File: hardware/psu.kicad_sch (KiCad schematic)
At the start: 57 parts, among them J6 Barrel_Jack_Switch, Q3 CSD87503Q3E, Q4 CSD87503Q3E, U10 TLV62569ADRL, U4 TPS61022, U5 BQ25798RQMR

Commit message: Debugging LED added
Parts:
- R10, R11, R34, R35, R37, R38, R39, R40, R41, R42, R_INT1, R_QON1, R_SCL1, R_SDA1, R_TS1, R_TS3: footprint Resistor_SMD:R_0603_1608Metric -> Resistor_SMD:R_0805_2012Metric
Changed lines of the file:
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@@
 			)
 		)
-		(property "Footprint" "Resistor_SMD:R_0603_1608Metric"
+		(property "Footprint" "Resistor_SMD:R_0805_2012Metric"
 			(at 196.088 64.77 90)
 			(effects
@@
 			)
 		)
-		(property "Footprint" "Resistor_SMD:R_0603_1608Metric"
+		(property "Footprint" "Resistor_SMD:R_0805_2012Metric"
 			(at 199.898 36.83 90)
 			(effects
@@
 			)
 		)
-		(property "Footprint" "Resistor_SMD:R_0603_1608Metric"
+		(property "Footprint" "Resistor_SMD:R_0805_2012Metric"
 			(at 76.2 68.072 90)
 			(effects
@@
 			)
 		)
-		(property "Footprint" "Resistor_SMD:R_0603_1608Metric"
+		(property "Footprint" "Resistor_SMD:R_0805_2012Metric"
 			(at 82.042 173.99 90)
 			(effects
@@
 			)
 		)
-		(property "Footprint" "Resistor_SMD:R_0603_1608Metric"
+		(property "Footprint" "Resistor_SMD:R_0805_2012Metric"
 			(at 31.242 55.88 90)
 			(effects
@@
 			)
 		)
-		(property "Footprint" "Resistor_SMD:R_0603_1608Metric"
+		(property "Footprint" "Resistor_SMD:R_0805_2012Metric"
 			(at 179.832 148.59 90)
 			(effects
@@
 			)
 		)
-		(property "Footprint" "Resistor_SMD:R_0603_1608Metric"
+		(property "Footprint" "Resistor_SMD:R_0805_2012Metric"
 			(at 82.042 185.42 90)
 			(effects
@@
 			)
 		)
-		(property "Footprint" "Resistor_SMD:R_0603_1608Metric"
+		(property "Footprint" "Resistor_SMD:R_0805_2012Metric"
 			(at 98.552 101.6 90)
 			(effects
@@
 			)
 		)
-		(property "Footprint" "Resistor_SMD:R_0603_1608Metric"
+		(property "Footprint" "Resistor_SMD:R_0805_2012Metric"
 			(at 256.032 29.21 90)
 			(effects
@@
 			)
 		)
-		(property "Footprint" "Resistor_SMD:R_0603_1608Metric"
+		(property "Footprint" "Resistor_SMD:R_0805_2012Metric"
 			(at 120.142 101.6 90)
 			(effects
@@
 			)
 		)
-		(property "Footprint" "Resistor_SMD:R_0603_1608Metric"
+		(property "Footprint" "Resistor_SMD:R_0805_2012Metric"
 			(at 179.832 137.16 90)
 			(effects
@@
 			)
 		)
-		(property "Footprint" "Resistor_SMD:R_0603_1608Metric"
+		(property "Footprint" "Resistor_SMD:R_0805_2012Metric"
 			(at 187.96 46.482 90)
 			(effects
@@
 			)
 		)
-		(property "Footprint" "Resistor_SMD:R_0603_1608Metric"
+		(property "Footprint" "Resistor_SMD:R_0805_2012Metric"
 			(at 265.43 23.622 90)
 			(effects
@@
 			)
 		)
-		(property "Footprint" "Resistor_SMD:R_0603_1608Metric"
+		(property "Footprint" "Resistor_SMD:R_0805_2012Metric"
 			(at 131.572 101.6 90)
 			(effects
@@
 			)
 		)
-		(property "Footprint" "Resistor_SMD:R_0603_1608Metric"
+		(property "Footprint" "Resistor_SMD:R_0805_2012Metric"
 			(at 108.712 101.6 90)
 			(effects
@@
 			)
 		)
-		(property "Footprint" "Resistor_SMD:R_0603_1608Metric"
+		(property "Footprint" "Resistor_SMD:R_0805_2012Metric"
 			(at 76.2 20.828 90)
 			(effects

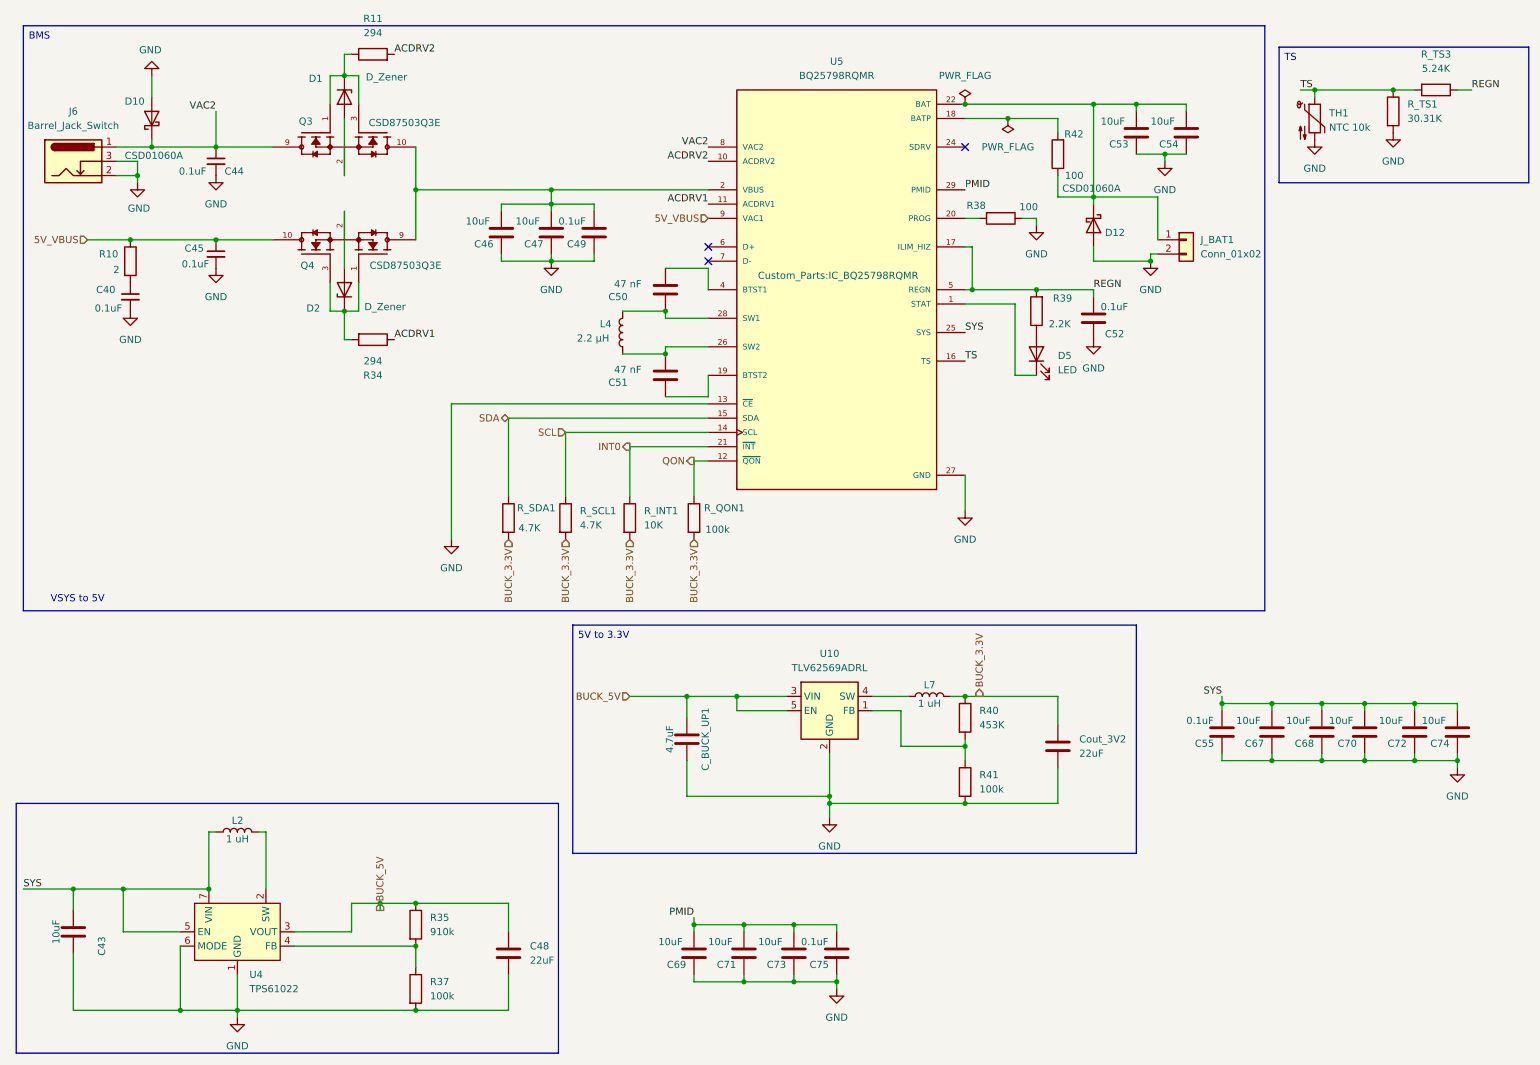
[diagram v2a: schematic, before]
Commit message: Added thermistor connection
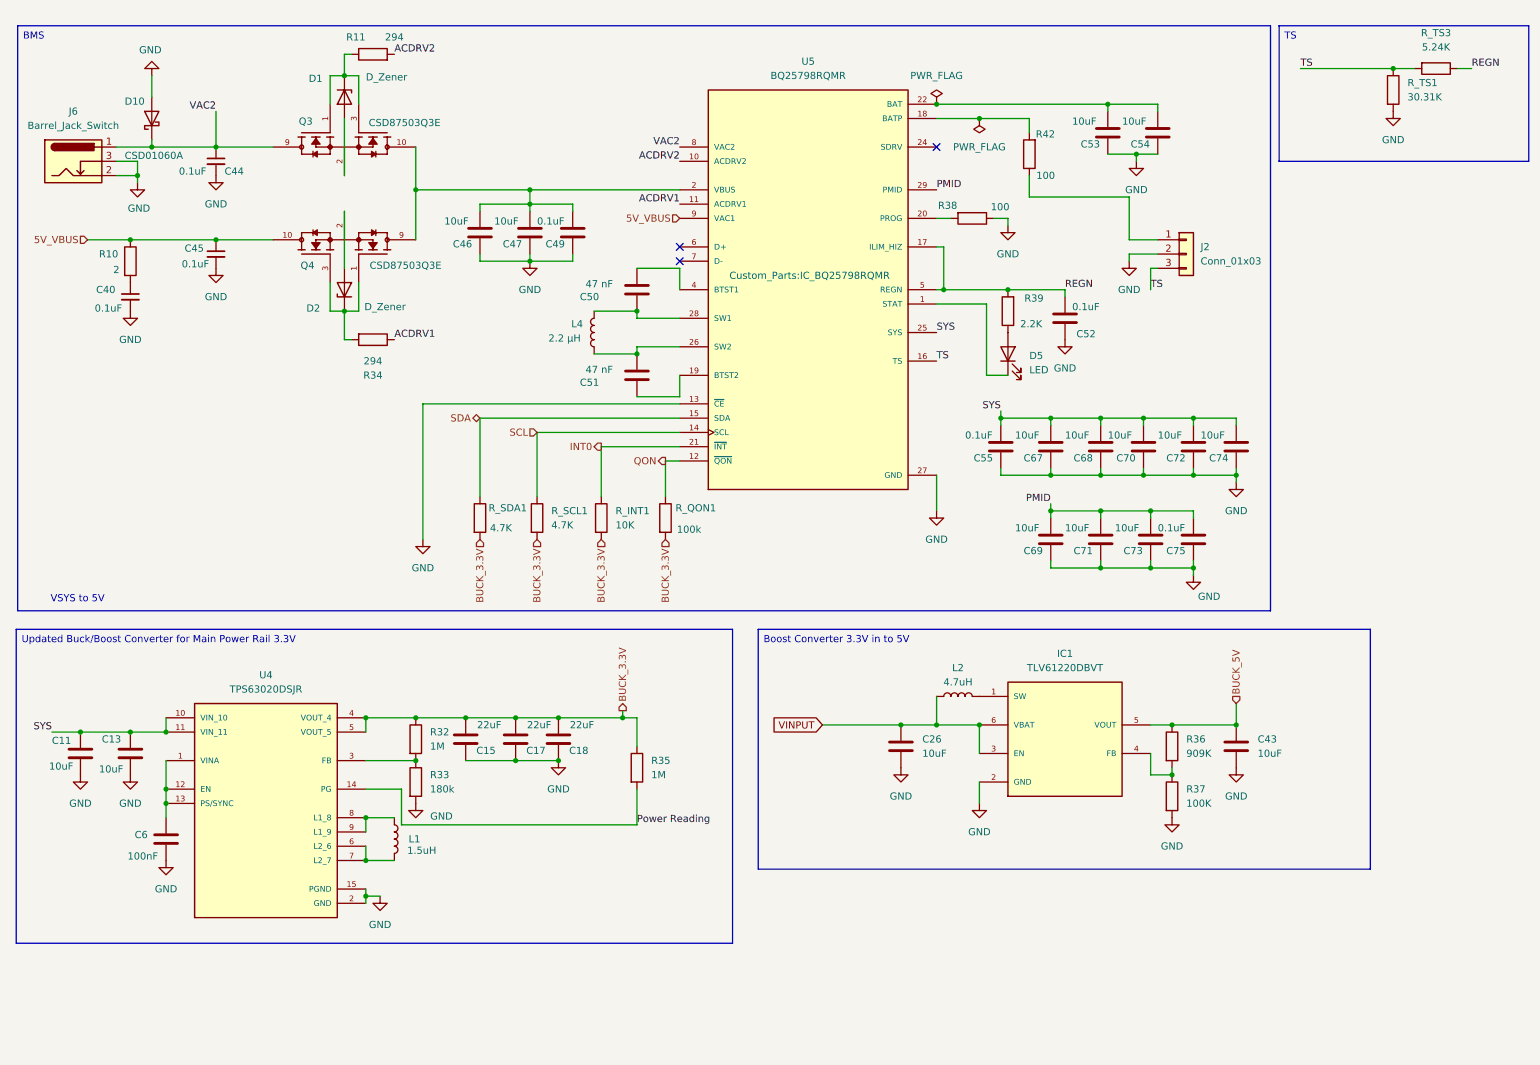
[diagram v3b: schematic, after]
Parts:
- removed C48, Cout_3V2: 22uF, Capacitor_SMD:C_0603_1608Metric, symbol Device:C
- removed C_BUCK_UP1: 4.7uF, Capacitor_SMD:C_0603_1608Metric, symbol Device:C
- removed D12: CSD01060A, Package_TO_SOT_THT:TO-220-2_Vertical, symbol Diode:CSD01060A
- removed J_BAT1: Conn_01x02, Connector_PinHeader_1.27mm:PinHeader_1x02_P1.27mm_Vertical, symbol Connector_Generic:Conn_01x02
- removed L7: 1 uH, Inductor_SMD:L_7.3x7.3_H3.5, symbol Device:L
- removed R40: 453K, Resistor_SMD:R_0805_2012Metric, symbol Device:R
- removed R41: 100k, Resistor_SMD:R_0805_2012Metric, symbol Device:R
- removed TH1: NTC 10k, Resistor_SMD:R_0603_1608Metric, symbol Device:Thermistor_NTC
- removed U10: TLV62569ADRL, Package_TO_SOT_SMD:SOT-563, symbol Regulator_Switching:TLV62569ADRL
- removed U4: TPS61022, Package_DFN_QFN:Texas_RWU0007A_VQFN-7_2x2mm_P0.5mm, symbol Converter_DCDC:TPS61022
- added C11, C13, C26: 10uF, symbol Device:C
- added C15, C17, C18: 22uF, symbol Device:C
- added C6: 100nF, symbol Device:C
- added IC1: TLV61220DBVT, symbol TLV61220DBVT:TLV61220DBVT
- added J2: Conn_01x03, Connector_JST:JST_PH_S3B-PH-K_1x03_P2.00mm_Horizontal, symbol Connector_Generic:Conn_01x03
- added L1: 1.5uH, symbol Device:L
- added R32: 1M, symbol Device:R
- added R33: 180k, symbol Device:R
- added R36: 909K, symbol Device:R
- added U4: TPS63020DSJR, TPS63020DSJR:IC_TPS63020DSJR, symbol TPS63020DSJR:TPS63020DSJR
- C43: footprint Capacitor_SMD:C_0603_1608Metric -> (none)
- L2: value 1 uH -> 4.7uH; footprint Inductor_SMD:L_7.3x7.3_H3.5 -> (none)
- R35: value 910k -> 1M; footprint Resistor_SMD:R_0805_2012Metric -> (none)
- R37: value 100k -> 100K; footprint Resistor_SMD:R_0805_2012Metric -> (none)
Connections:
- net BAT: no longer R42.1
- net BUCK_3.3V: now also R35.1, C15.2, C17.2, C18.2, R32.1, U4.4 (VOUT_4), U4.5 (VOUT_5)
- net BUCK_5V: now also C43.1, IC1.5 (VOUT), R36.1; no longer R35.1
- net GND: now also C11.2, C13.2, C15.1, C17.1, C18.1, C26.2, C6.2, IC1.2 (GND), J2.2 (Pin_2), R33.2, U4.15 (PGND), U4.2 (GND)
- net SYS: now also C11.1, C13.1, U4.10 (VIN_10), U4.11 (VIN_11); no longer C43.1, L2.1
- net TS: now also J2.3 (Pin_3)
- net at L2.2: now also IC1.1 (SW)
- net at R37.1: now also IC1.4 (FB), R36.2; no longer R35.2
- new net: J2.1 (Pin_1), R42.1
- new net: R32.2, R33.1, U4.3 (FB)
- new net: C6.1, U4.1 (VINA), U4.12 (EN), U4.13 (PS/SYNC)
- new net: L1.1, U4.8 (L1_8), U4.9 (L1_9)
- new net: L1.2, U4.6 (L2_6), U4.7 (L2_7)
- new net Power Reading: R35.2, U4.14 (PG)
- new net VINPUT: C26.1, IC1.3 (EN), IC1.6 (VBAT), L2.1
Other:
- moved on the sheet: C46, C47, C49, C50, C51, C52, C53, C54, C55, C67, C68, C69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

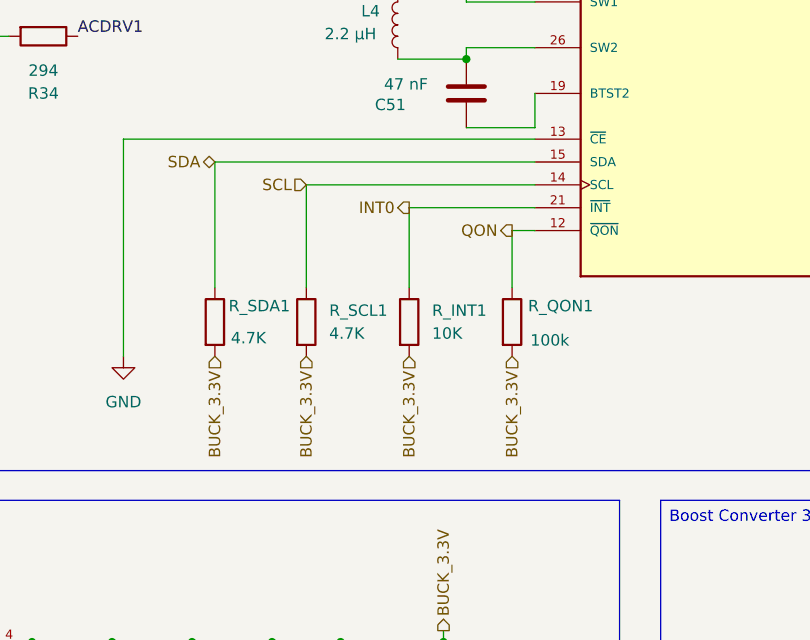
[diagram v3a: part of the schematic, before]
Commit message: Unified I2C pull-ups to MCU page
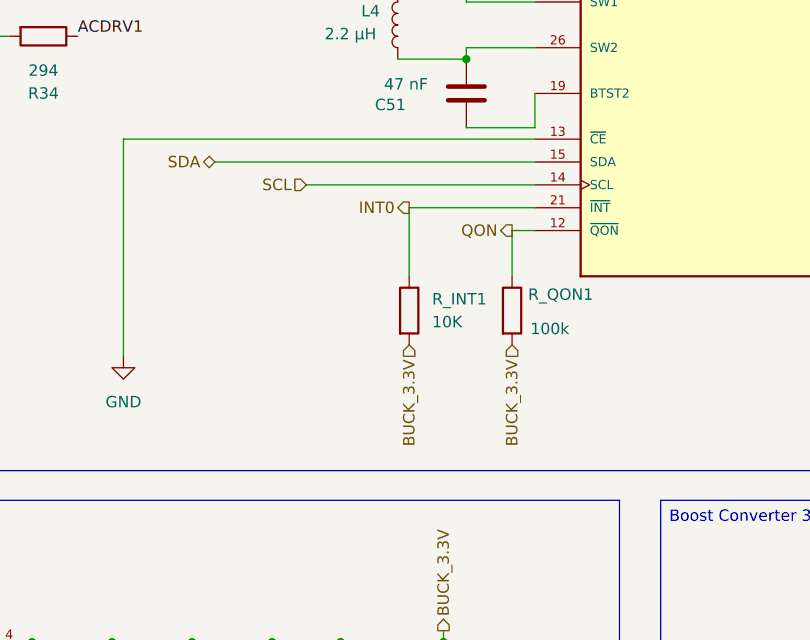
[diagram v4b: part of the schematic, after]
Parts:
- removed R_SCL1, R_SDA1: 4.7K, Resistor_SMD:R_0805_2012Metric, symbol Device:R
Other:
- moved on the sheet: R_INT1, R_QON1
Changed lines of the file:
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@@
 	(wire
 		(pts
-			(xy 116.84 88.9) (xy 116.84 97.79)
+			(xy 116.84 88.9) (xy 116.84 96.52)
 		)
 		(stroke
@@
 	(wire
 		(pts
-			(xy 105.41 86.36) (xy 105.41 97.79)
-		)
-		(stroke
-			(width 0)
-			(type default)
-		)
-	)
-	(wire
-		(pts
 			(xy 104.14 45.72) (xy 111.76 45.72)
 		)
@@
 	(wire
 		(pts
-			(xy 128.27 97.79) (xy 128.27 91.44)
+			(xy 128.27 96.52) (xy 128.27 91.44)
 		)
 		(stroke
@@
 	(wire
 		(pts
-			(xy 95.25 83.82) (xy 95.25 97.79)
-		)
-		(stroke
-			(width 0)
-			(type default)
-		)
-	)
-	(wire
-		(pts
 			(xy 123.19 57.15) (xy 130.81 57.15)
 		)
@@
 		)
 	)
-	(hierarchical_label "BUCK_3.3V"
-		(shape input)
-		(at 95.25 105.41 270)
-		(effects
-			(font
-				(size 1.27 1.27)
-			)
-			(justify right)
-		)
-	)
-	(hierarchical_label "BUCK_3.3V"
-		(shape input)
-		(at 105.41 105.41 270)
-		(effects
-			(font
-				(size 1.27 1.27)
-			)
-			(justify right)
-		)
-	)
 	(hierarchical_label "SDA"
 		(shape bidirectional)
@@
 	(hierarchical_label "BUCK_3.3V"
 		(shape input)
-		(at 116.84 105.41 270)
+		(at 116.84 104.14 270)
 		(effects
 			(font
@@
 	(hierarchical_label "BUCK_3.3V"
 		(shape input)
-		(at 128.27 105.41 270)
+		(at 128.27 104.14 270)
 		(effects
 			(font
@@
 	(symbol
 		(lib_id "Device:R")
-		(at 95.25 101.6 0)
-		(unit 1)
-		(exclude_from_sim no)
-		(in_bom yes)
-		(on_board yes)
-		(dnp no)
-		(property "Reference" "R_SDA1"
-			(at 96.774 99.822 0)
-			(effects
-				(font
-					(size 1.27 1.27)
-				)
-				(justify left)
-			)
-		)
-		(property "Value" "4.7K"
-			(at 97.028 103.378 0)
-			(effects
-				(font
-					(size 1.27 1.27)
-				)
-				(justify left)
-			)
-		)
-		(property "Footprint" "Resistor_SMD:R_0805_2012Metric"
-			(at 93.472 101.6 90)
-			(effects
-				(font
-					(size 1.27 1.27)
-				)
-				(hide yes)
-			)
-		)
-		(property "Datasheet" "~"
-			(at 95.25 101.6 0)
-			(effects
-				(font
-					(size 1.27 1.27)
-				)
-				(hide yes)
-			)
-		)
-		(property "Description" "Resistor"
-			(at 95.25 101.6 0)
-			(effects
-				(font
-					(size 1.27 1.27)
-				)
-				(hide yes)
-			)
-		)
-		(pin "2"
-		)
-		(pin "1"
-		)
-		(instances
-			(project "Senior_Design"
-				(path "/8f5928e8-0fc1-4443-a20f-3bfeb956761e/09dae378-4d12-4dca-bc21-c216f94ec21f"
-					(reference "R_SDA1")
-					(unit 1)
-				)
-			)
-		)
-	)
-	(symbol
-		(lib_id "Device:R")
 		(at 257.81 25.4 0)
 		(unit 1)
@@
 	(symbol
 		(lib_id "Device:R")
-		(at 116.84 101.6 0)
+		(at 116.84 100.33 0)
 		(unit 1)
 		(exclude_from_sim no)
@@
 		(fields_autoplaced yes)
 		(property "Reference" "R_INT1"
-			(at 119.38 100.3299 0)
+			(at 119.38 99.0599 0)
 			(effects
 				(font
@@
 		)
 		(property "Value" "10K"
-			(at 119.38 102.8699 0)
+			(at 119.38 101.5999 0)
 			(effects
 				(font
@@
 		)
 		(property "Footprint" "Resistor_SMD:R_0805_2012Metric"
-			(at 115.062 101.6 90)
+			(at 115.062 100.33 90)
 			(effects
 				(font
@@
 		)
 		(property "Datasheet" "~"
-			(at 116.84 101.6 0)
+			(at 116.84 100.33 0)
 			(effects
 				(font
@@
 		)
 		(property "Description" "Resistor"
-			(at 116.84 101.6 0)
+			(at 116.84 100.33 0)
 			(effects
 				(font
@@
 	(symbol
 		(lib_id "Device:R")
-		(at 128.27 101.6 0)
+		(at 128.27 100.33 0)
 		(unit 1)
 		(exclude_from_sim no)
@@
 		(dnp no)
 		(property "Reference" "R_QON1"
-			(at 130.048 99.822 0)
+			(at 130.048 98.552 0)
 			(effects
 				(font
@@
 		)
 		(property "Value" "100k"
-			(at 130.302 103.632 0)
+			(at 130.302 102.362 0)
 			(effects
 				(font
@@
 		)
 		(property "Footprint" "Resistor_SMD:R_0805_2012Metric"
-			(at 126.492 101.6 90)
+			(at 126.492 100.33 90)
 			(effects
 				(font
@@
 		)
 		(property "Datasheet" "~"
-			(at 128.27 101.6 0)
+			(at 128.27 100.33 0)
 			(effects
 				(font
@@
 		)
 		(property "Description" "Resistor"
-			(at 128.27 101.6 0)
+			(at 128.27 100.33 0)
 			(effects
 				(font
@@
 					(unit 1)
 				)
-			)
-		)
-	)
-	(symbol
-		(lib_id "Device:R")
-		(at 105.41 101.6 0)
-		(unit 1)
-		(exclude_from_sim no)
-		(in_bom yes)
-		(on_board yes)
-		(dnp no)
-		(fields_autoplaced yes)
-		(property "Reference" "R_SCL1"
-			(at 107.95 100.3299 0)
-			(effects
-				(font
-					(size 1.27 1.27)
-				)
-				(justify left)
-			)
-		)
-		(property "Value" "4.7K"
-			(at 107.95 102.8699 0)
-			(effects
-				(font
-					(size 1.27 1.27)
-				)
-				(justify left)
-			)
-		)
-		(property "Footprint" "Resistor_SMD:R_0805_2012Metric"
-			(at 103.632 101.6 90)
-			(effects
-				(font
-					(size 1.27 1.27)
-				)
-				(hide yes)
-			)
-		)
-		(property "Datasheet" "~"
-			(at 105.41 101.6 0)
-			(effects
-				(font
-					(size 1.27 1.27)
-				)
-				(hide yes)
-			)
-		)
-		(property "Description" "Resistor"
-			(at 105.41 101.6 0)
-			(effects
-				(font
-					(size 1.27 1.27)
-				)
-				(hide yes)
-			)
-		)
-		(pin "2"
-		)
-		(pin "1"
-		)
-		(instances
-			(project "Senior_Design"
-				(path "/8f5928e8-0fc1-4443-a20f-3bfeb956761e/09dae378-4d12-4dca-bc21-c216f94ec21f"
-					(reference "R_SCL1")
-					(unit 1)
-				)

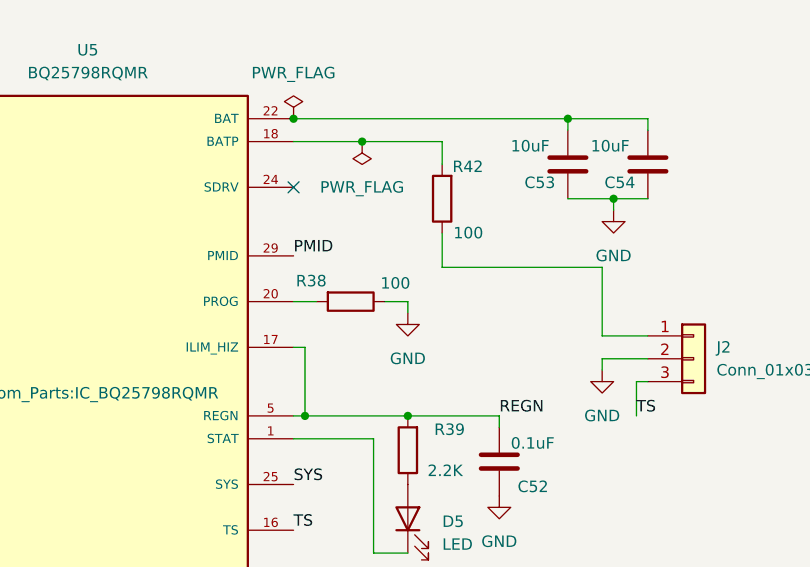
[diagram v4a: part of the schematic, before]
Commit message: MCU Reset Pin fix
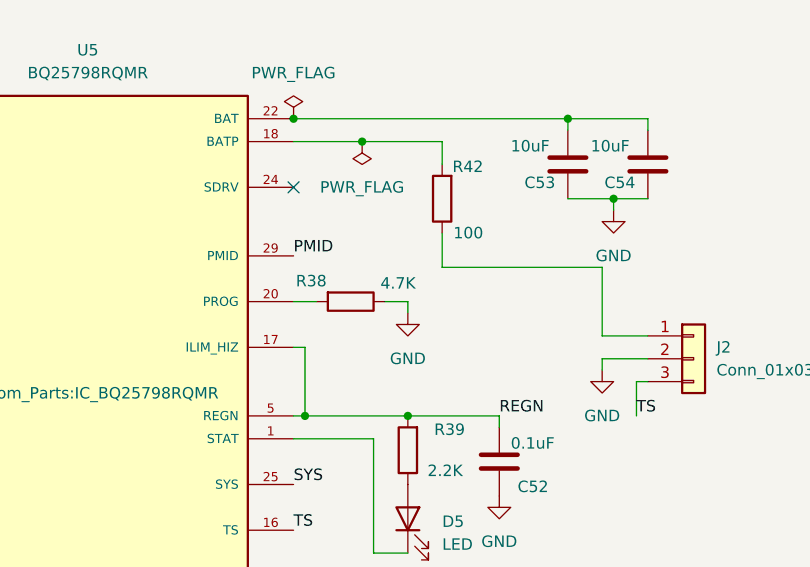
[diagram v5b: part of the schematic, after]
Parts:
- R38: value 100 -> 4.7K
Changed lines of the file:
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@@
 			)
 		)
-		(property "Value" "100"
+		(property "Value" "4.7K"
 			(at 186.182 46.228 90)
 			(effects
